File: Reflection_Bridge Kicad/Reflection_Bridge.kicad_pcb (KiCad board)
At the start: 2 copper layers, 13.4 x 20.5 mm, 7 parts, among them P1 SMA_Female, P2 SMA_Female, P3 SMA_Female, T1 Transformer_1P_1S

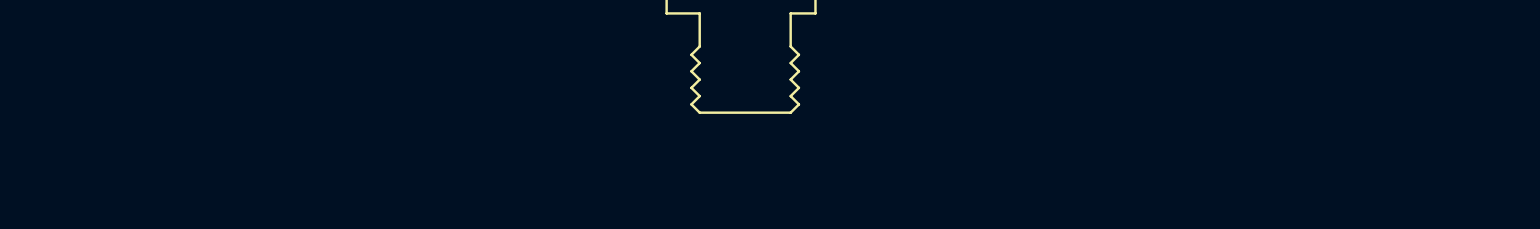
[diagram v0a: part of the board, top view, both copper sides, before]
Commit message: Added notes to fix T1 footprint on the reflection bridge.
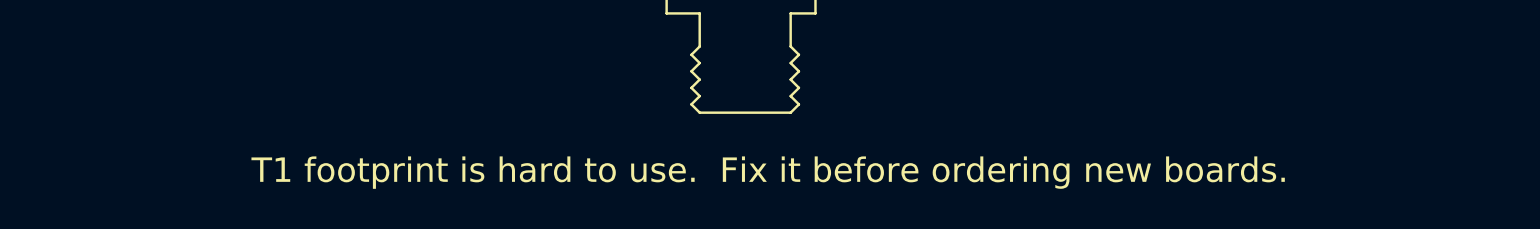
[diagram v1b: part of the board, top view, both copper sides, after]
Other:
- board text added: "T1 footprint is hard to use. Fix it before ordering new boards."
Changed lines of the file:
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@@
-(kicad_pcb (version 20171130) (host pcbnew 5.0.0-fee4fd1~66~ubuntu18.04.1)
+(kicad_pcb (version 20171130) (host pcbnew 5.1.2-f72e74a~84~ubuntu19.04.1)
   (general
     (thickness 1.6)
-    (drawings 14)
+    (drawings 15)
     (tracks 62)
     (zones 0)
@@
     (zone_45_only no)
     (trace_min 0.2)
-    (segment_width 0.2)
-    (edge_width 0.15)
     (via_size 0.8)
     (via_drill 0.4)
@@
     (uvia_min_size 0.2)
     (uvia_min_drill 0.1)
+    (edge_width 0.15)
+    (segment_width 0.2)
     (pcb_text_width 0.3)
     (pcb_text_size 1.5 1.5)
@@
       (net 3 "Net-(P2-Pad1)"))
   )
+  (gr_text "T1 footprint is hard to use.  Fix it before ordering new boards." (at 85.598 87.122) (layer F.SilkS)
+    (effects (font (size 1.5 1.5) (thickness 0.3)))
+  )
   (gr_text Bridge (at 82.9 62.65) (layer B.SilkS)

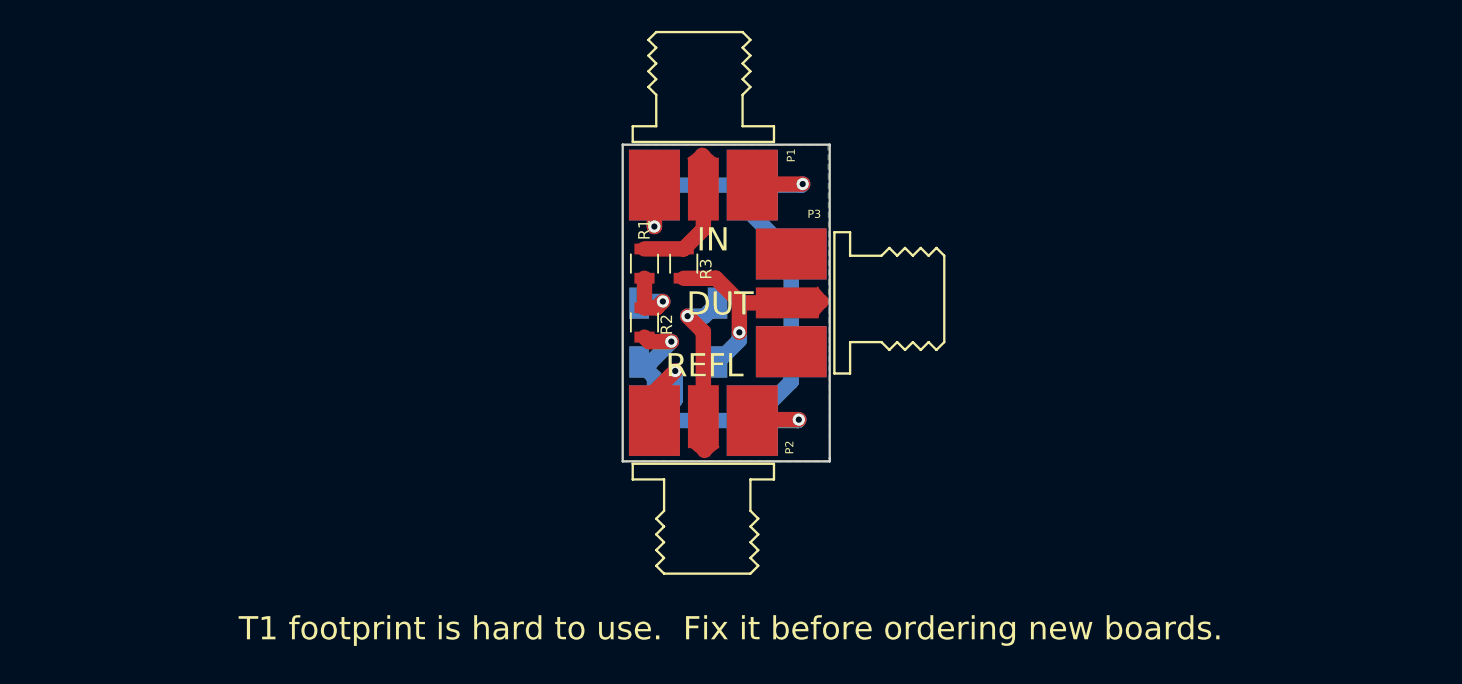
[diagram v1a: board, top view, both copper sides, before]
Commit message: Added v0.2 of reflection bridge.
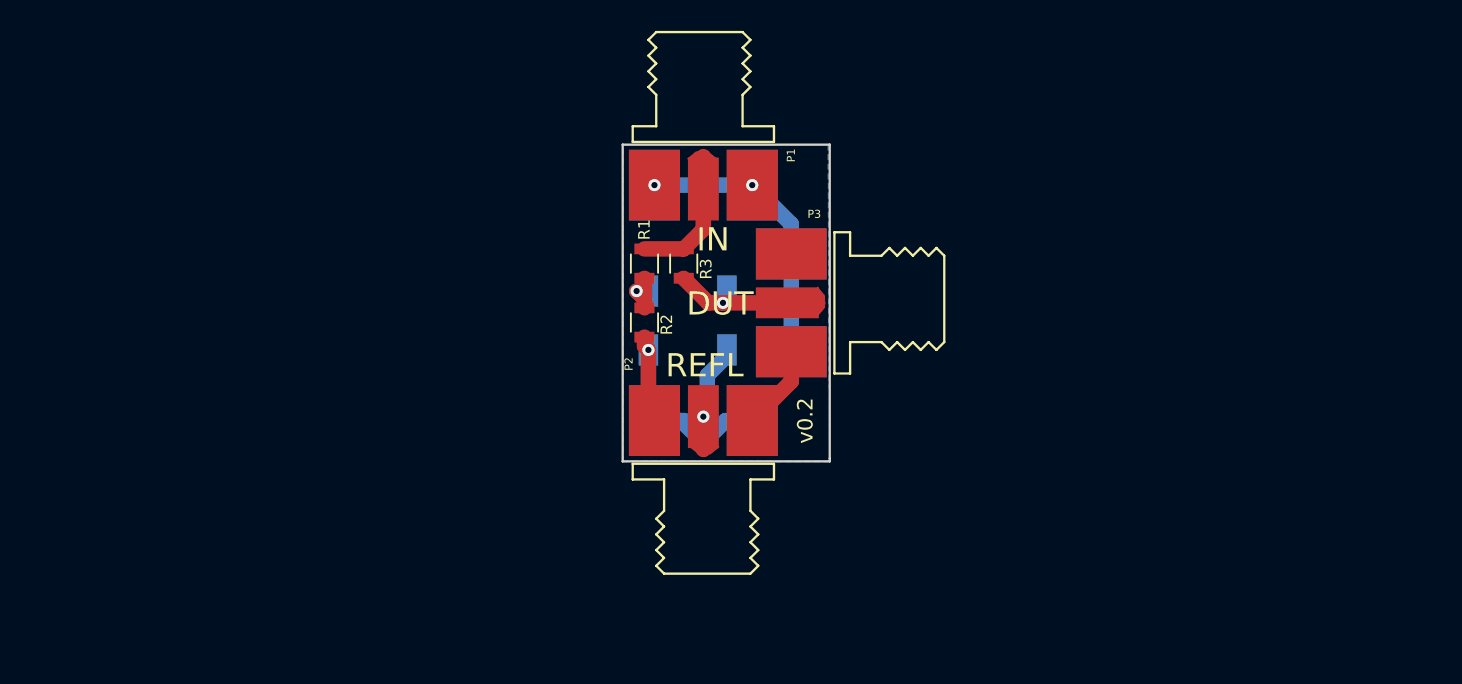
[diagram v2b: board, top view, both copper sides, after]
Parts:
- moved T1 0.99 mm to (82.8, 67.8)
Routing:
- net GND: track 64.3 -> 43.1 mm, vias 5 -> 3
- net Net-(P2-Pad1): track 11.4 -> 7.07 mm
- net Net-(P3-Pad1): track 14.0 -> 10.2 mm
- net Net-(R1-Pad2): track 4.86 -> 3.39 mm
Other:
- board text added: "v0.2"
- board text removed: "T1 footprint is hard to use. Fix it before ordering new boards."
